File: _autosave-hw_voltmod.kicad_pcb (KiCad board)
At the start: 2 copper layers, 70 x 50 mm, 96 parts, among them J1 Conn_01x09_Pin, J2 Conn_01x05_Pin, J3 Conn_01x04_Pin, U1 L78L33_SO8, U2 STM32G071KBTx, U3 TL074, U4 TL074

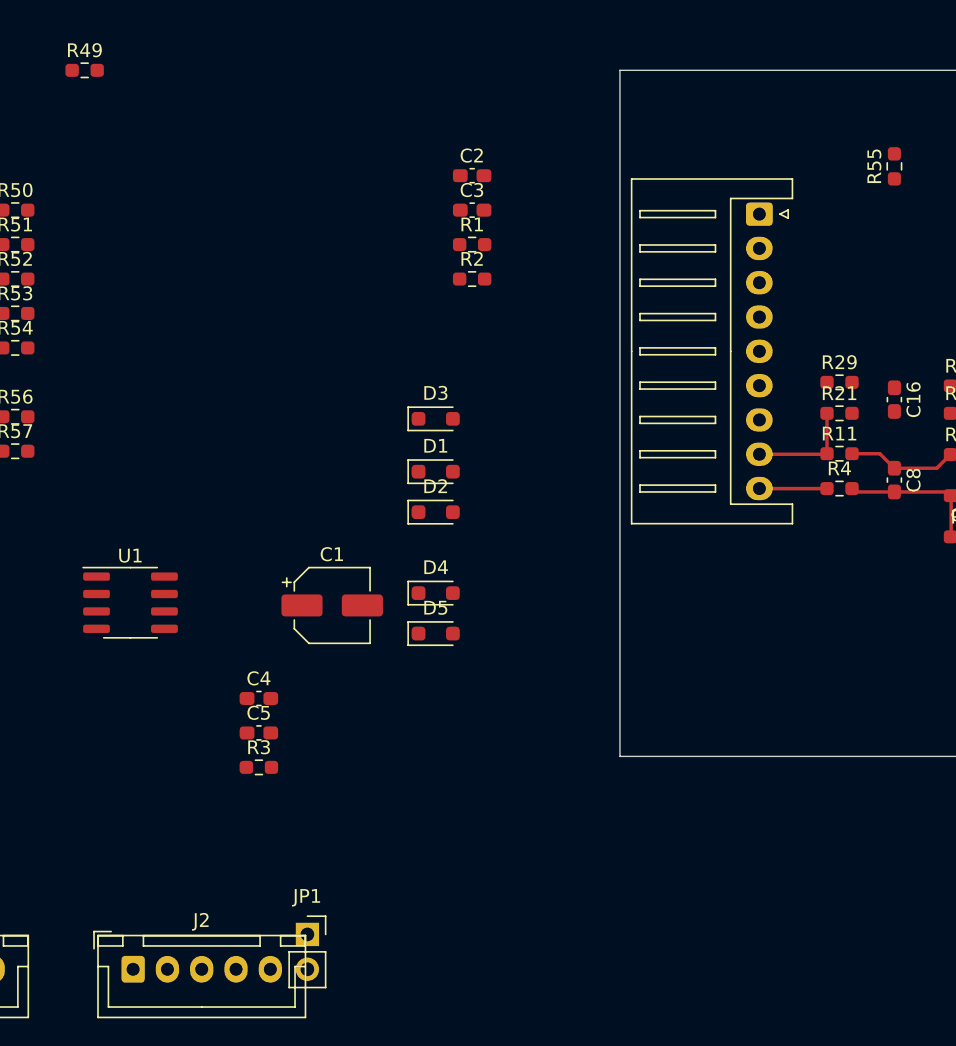
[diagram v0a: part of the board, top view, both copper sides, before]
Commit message: aisler DRC und preise
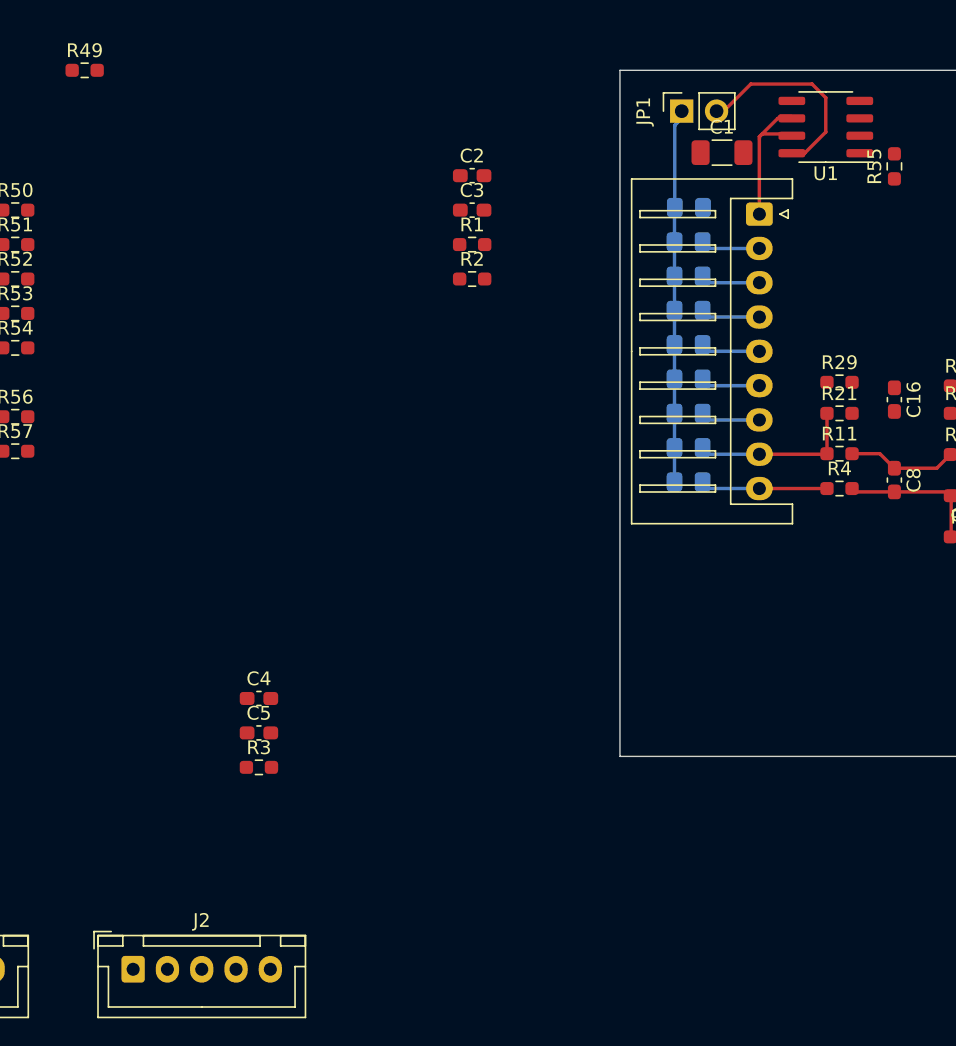
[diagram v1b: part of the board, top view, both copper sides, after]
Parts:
- added D6: BAT41, Diode_SMD:D_0805_2012Metric_Pad1.15x1.40mm_HandSolder, B.Cu at (5.00, 17.5)
- added D7: BAT41, Diode_SMD:D_0805_2012Metric_Pad1.15x1.40mm_HandSolder, B.Cu at (5.00, 22.5)
- added D8: BAT41, Diode_SMD:D_0805_2012Metric_Pad1.15x1.40mm_HandSolder, B.Cu at (5.00, 27.5)
- added D9: BAT41, Diode_SMD:D_0805_2012Metric_Pad1.15x1.40mm_HandSolder, B.Cu at (5.00, 12.5)
- C1: footprint Capacitor_SMD:CP_Elec_5x3 -> Capacitor_SMD:C_1206_3216Metric_Pad1.33x1.80mm_HandSolder
- D1, D2, D3, D4, D5: footprint Diode_SMD:D_SOD-323_HandSoldering -> Diode_SMD:D_0805_2012Metric_Pad1.15x1.40mm_HandSolder; moved to B.Cu
- moved JP1 65.9 mm to (4.50, 2.98), turned to 90 degrees
- moved U1 61.4 mm to (15.0, 4.13), turned to 180 degrees
- moved C1 43.5 mm to (7.44, 6.00)
- moved D5 31.9 mm to (5.00, 15.0)
- moved D1 26.7 mm to (5.03, 10.0)
- moved D4 25.8 mm to (5.00, 20.0)
- moved D2 18.6 mm to (5.00, 30.0)
- moved D3 18.4 mm to (5.00, 25.0)
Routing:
- net Net-(D1-K): track 0.00 -> 26.7 mm
- net VBUS: track 0.00 -> 15.0 mm
- net GNDD: track 0.00 -> 12.0 mm
- net /Level Shifter/cell8: track 4.93 -> 9.26 mm
- net /Level Shifter/cell7: track 7.88 -> 12.2 mm
- net /Level Shifter/cell6: track 0.00 -> 4.33 mm
- net /Level Shifter/cell5: track 0.00 -> 4.33 mm
- net /Level Shifter/cell4: track 0.00 -> 4.33 mm
- net /Level Shifter/cell3: track 0.00 -> 4.33 mm
- net /Level Shifter/cell2: track 0.00 -> 4.33 mm
- net /Level Shifter/cell1: track 0.00 -> 4.33 mm
